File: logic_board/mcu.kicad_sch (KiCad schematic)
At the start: 4 parts, among them J1 SJ3-35083C-TR, J2 SOICBite, U1 STM32H7B0RBTx, U3 MCP73832-2-OT

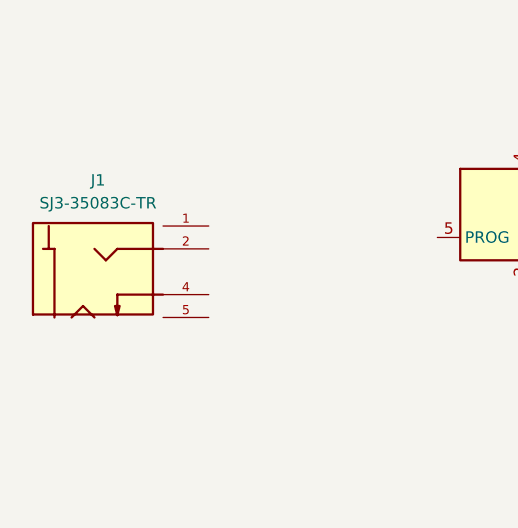
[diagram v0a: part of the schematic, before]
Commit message: Create a pin mapping file
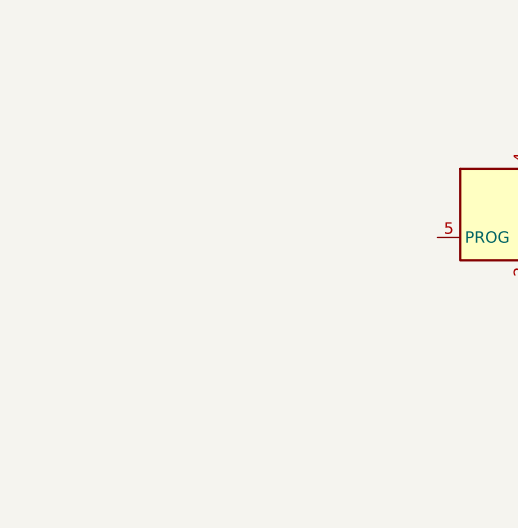
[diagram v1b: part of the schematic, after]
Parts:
- removed J1: SJ3-35083C-TR, Custom_Footprints:SAMESKY_SJ3-35083C-TR, symbol Custom_Symbols:SJ3-35083C-TR
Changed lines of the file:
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@@
-	)
-	(symbol
-		(lib_id "Custom_Symbols:SJ3-35083C-TR")
-		(at 40.64 63.5 0)
-		(unit 1)
-		(exclude_from_sim no)
-		(in_bom yes)
-		(on_board yes)
-		(dnp no)
-		(fields_autoplaced yes)
-		(property "Reference" "J1"
-			(at 38.4934 53.34 0)
-			(effects
-				(font
-					(size 1.27 1.27)
-				)
-			)
-		)
-		(property "Value" "SJ3-35083C-TR"
-			(at 38.4934 55.88 0)
-			(effects
-				(font
-					(size 1.27 1.27)
-				)
-			)
-		)
-		(property "Footprint" "Custom_Footprints:SAMESKY_SJ3-35083C-TR"
-			(at 40.64 63.5 0)
-			(effects
-				(font
-					(size 1.27 1.27)
-				)
-				(justify bottom)
-				(hide yes)
-			)
-		)
-		(property "Datasheet" "https://www.sameskydevices.com/product/resource/sj3-3508x.pdf"
-			(at 40.64 63.5 0)
-			(effects
-				(font
-					(size 1.27 1.27)
-				)
-				(hide yes)
-			)
-		)
-		(property "Description" "3.5mm Audio Jack"
-			(at 40.64 63.5 0)
-			(effects
-				(font
-					(size 1.27 1.27)
-				)
-				(hide yes)
-			)
-		)
-		(property "PARTREV" "1.01"
-			(at 40.64 63.5 0)
-			(effects
-				(font
-					(size 1.27 1.27)
-				)
-				(justify bottom)
-				(hide yes)
-			)
-		)
-		(property "STANDARD" "Manufacturer Recommendations"
-			(at 40.64 63.5 0)
-			(effects
-				(font
-					(size 1.27 1.27)
-				)
-				(justify bottom)
-				(hide yes)
-			)
-		)
-		(property "MAXIMUM_PACKAGE_HEIGHT" "5.3mm"
-			(at 40.64 63.5 0)
-			(effects
-				(font
-					(size 1.27 1.27)
-				)
-				(justify bottom)
-				(hide yes)
-			)
-		)
-		(property "MANUFACTURER" "Same Sky"
-			(at 40.64 63.5 0)
-			(effects
-				(font
-					(size 1.27 1.27)
-				)
-				(justify bottom)
-				(hide yes)
-			)
-		)
-		(pin "1"
-		)
-		(pin "2"
-		)
-		(pin "4"
-		)
-		(pin "5"
-		)
-		(instances
-			(project "logic_board"
-				(path "/b7b37fe1-b409-497a-9440-d94d882f6459/bab78c00-64d8-4e72-b9b2-c8e2bf935ca1"
-					(reference "J1")
-					(unit 1)
-				)
-			)
-		)
 	)
 	(symbol

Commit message: Add more parts to schematic
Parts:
- added J3: USB_C_Receptacle_USB2.0_16P, Custom_Footprints:TYPE-C-31-M-12, symbol Connector:USB_C_Receptacle_USB2.0_16P
- added J5: Conn_01x02, Connector_JST:JST_PH_B2B-PH-SM4-TB_1x02-1MP_P2.00mm_Vertical, symbol Connector_Generic:Conn_01x02
- added SW1, SW2, SW3, SW4: SW_Push, Button_Switch_SMD:SW_SPST_PTS645Sx43SMTR92, symbol Switch:SW_Push
- added SW5: SW_SPDT, Custom_Footprints:Alps Alpine SSSS211603, symbol Switch:SW_SPDT
- added U4: AP2112K-3.3, Package_TO_SOT_SMD:SOT-23-5, symbol Regulator_Linear:AP2112K-3.3
- added Y1: Crystal_GND24, Crystal:Crystal_SMD_3225-4Pin_3.2x2.5mm, symbol Device:Crystal_GND24
- J2: now left out of the parts list
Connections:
- new net: J3.A1 (GND), J3.A12 (GND), J3.B1 (GND), J3.B12 (GND)
- new net: J3.A4 (VBUS), J3.A9 (VBUS), J3.B4 (VBUS), J3.B9 (VBUS)
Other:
- moved on the sheet: U3

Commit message: Board and symbol updates.
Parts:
- SW5: LCSC part number (none) -> SSSS211603
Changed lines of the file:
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@@
+			)
+		)
+		(property "LCSC part number" "SSSS211603"
+			(at 110.49 121.92 0)
+			(effects
+				(font
+					(size 1.27 1.27)
+				)
+				(hide yes)
 			)
 		)

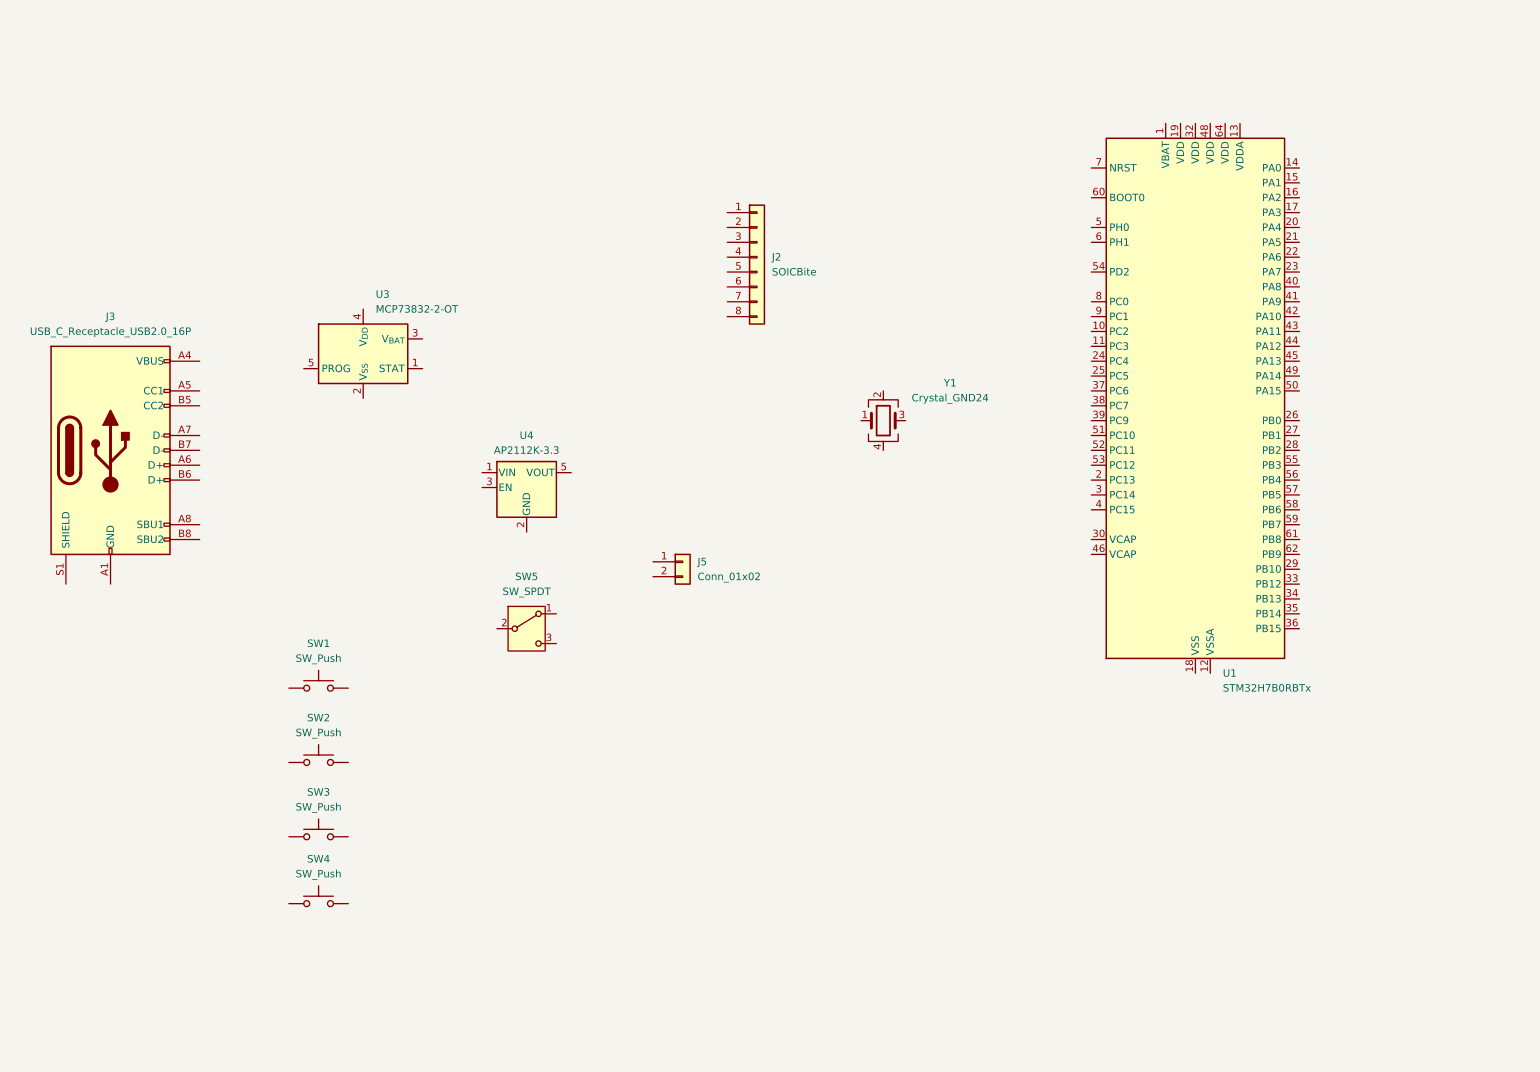
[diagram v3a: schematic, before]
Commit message: Ready for routing. - Lay out all components in proper positions - Add all support passives (bypass caps, etc) - Add board corner cutouts for enclosure bosses.
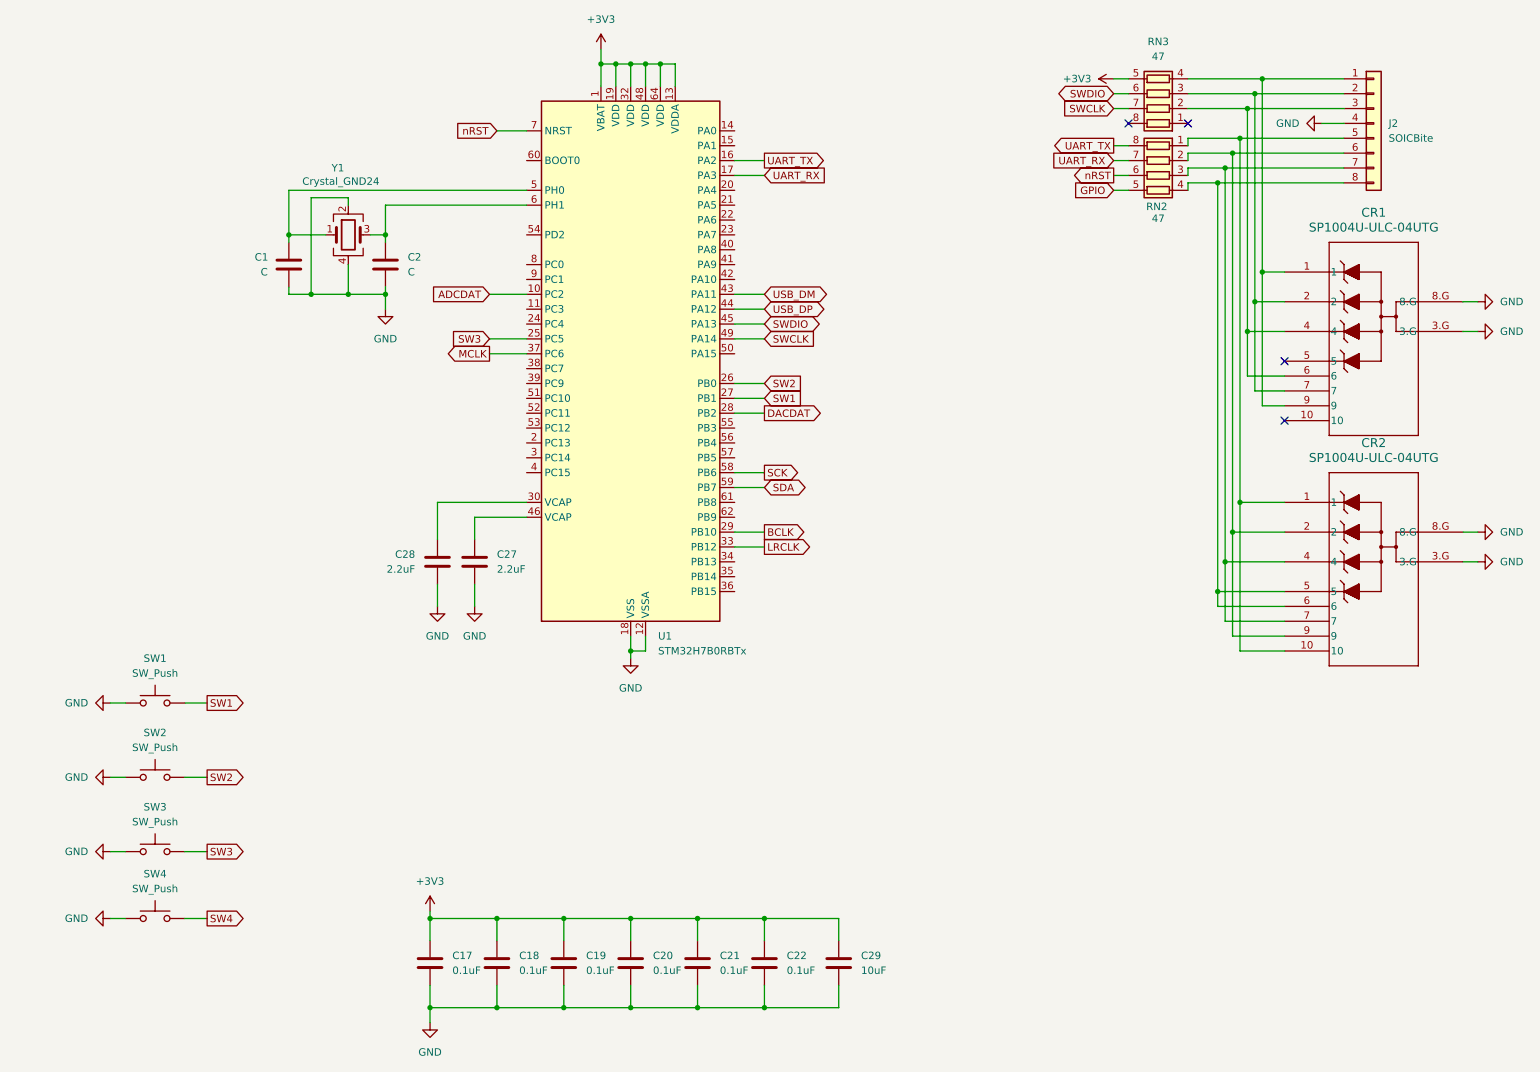
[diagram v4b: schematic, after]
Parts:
- removed J3: USB_C_Receptacle_USB2.0_16P, Custom_Footprints:TYPE-C-31-M-12, symbol Connector:USB_C_Receptacle_USB2.0_16P
- removed J5: Conn_01x02, Connector_JST:JST_PH_B2B-PH-SM4-TB_1x02-1MP_P2.00mm_Vertical, symbol Connector_Generic:Conn_01x02
- removed SW5: SW_SPDT, Custom_Footprints:Alps Alpine SSSS211603, symbol Switch:SW_SPDT
- removed U3: MCP73832-2-OT, Package_TO_SOT_SMD:SOT-23-5, symbol Battery_Management:MCP73832-2-OT
- removed U4: AP2112K-3.3, Package_TO_SOT_SMD:SOT-23-5, symbol Regulator_Linear:AP2112K-3.3
- added C1, C2: C, Capacitor_SMD:C_0603_1608Metric, symbol Device:C
- added C17, C18, C19, C20, C21, C22: 0.1uF, Capacitor_SMD:C_0603_1608Metric, symbol Device:C
- added C27, C28: 2.2uF, Capacitor_SMD:C_0603_1608Metric, symbol Device:C
- added C29: 10uF, Capacitor_SMD:C_0603_1608Metric, symbol Device:C
- added CR1, CR2: SP1004U-ULC-04UTG, Custom_Footprints:1004DFN_LTF, symbol Custom_Symbols:SP1004U-ULC-04UTG
- added RN2, RN3: 47, Resistor_SMD:R_Array_Concave_4x0402, symbol Device:R_Pack04
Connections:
- net at Y1.1: now also U1.5 (PH0), C1.1
- net GND: now reaches Y1.2
- net GND: now also J2.4 (Pin_4), SW1.1, SW2.1, SW3.1, SW4.1, U1.12 (VSSA), U1.18 (VSS), U1.31 (VSS), U1.47 (VSS), U1.63 (VSS), Y1.4, C1.2, C17.2, C18.2, C19.2, C2.2, C20.2, C21.2, C22.2, C27.2, C28.2, C29.2, CR1.3.G, CR1.8.G, CR2.3.G, CR2.8.G
- net at Y1.3: now also U1.6 (PH1), C2.1
- net +3V3: now reaches U1.1 (VBAT)
- net +3V3: now also U1.13 (VDDA), U1.19 (VDD), U1.32 (VDD), U1.48 (VDD), U1.64 (VDD), C17.1, C18.1, C19.1, C20.1, C21.1, C22.1, C29.1, RN3.5 (R4.2)
- net ADCDAT: now reaches U1.10 (PC2)
- net UART_TX: now reaches U1.16 (PA2)
- net UART_TX: now also RN2.8 (R1.2)
- net UART_RX: now reaches U1.17 (PA3)
- net UART_RX: now also RN2.7 (R2.2)
- net SW3: now reaches U1.25 (PC5)
- net SW3: now also SW3.2
- net SW2: now reaches U1.26 (PB0)
- net SW2: now also SW2.2
- net SW1: now reaches U1.27 (PB1)
- net SW1: now also SW1.2
- net DACDAT: now reaches U1.28 (PB2)
- net BCLK: now reaches U1.29 (PB10)
- net at U1.30 (VCAP): now also C28.1
- net LRCLK: now reaches U1.33 (PB12)
- net MCLK: now reaches U1.37 (PC6)
- net USB_DM: now reaches U1.43 (PA11)
- net USB_DP: now reaches U1.44 (PA12)
- net SWDIO: now reaches U1.45 (PA13)
- net SWDIO: now also RN3.6 (R3.2)
- net at U1.46 (VCAP): now also C27.1
- net SWCLK: now reaches U1.49 (PA14)
- net SWCLK: now also RN3.7 (R2.2)
- net SCK: now reaches U1.58 (PB6)
- net SDA: now reaches U1.59 (PB7)
- net nRST: now reaches U1.7 (NRST)
- net nRST: now also RN2.6 (R3.2)
- net SW4: now reaches SW4.2
- net at J2.1 (Pin_1): now also CR1.1, CR1.9, RN3.4 (R4.1)
- net at J2.2 (Pin_2): now also CR1.2, CR1.7, RN3.3 (R3.1)
- net at J2.3 (Pin_3): now also CR1.4, CR1.6, RN3.2 (R2.1)
- net at J2.5 (Pin_5): now also CR2.1, CR2.10, RN2.1 (R1.1)
- net at J2.6 (Pin_6): now also CR2.2, CR2.9, RN2.2 (R2.1)
- net at J2.7 (Pin_7): now also CR2.4, CR2.7, RN2.3 (R3.1)
- net at J2.8 (Pin_8): now also CR2.5, CR2.6, RN2.4 (R4.1)
- new net GPIO: RN2.5 (R4.2)
- no-connect marks 0 -> 4
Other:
- moved on the sheet: J2, SW1, SW2, SW3, SW4, U1, Y1

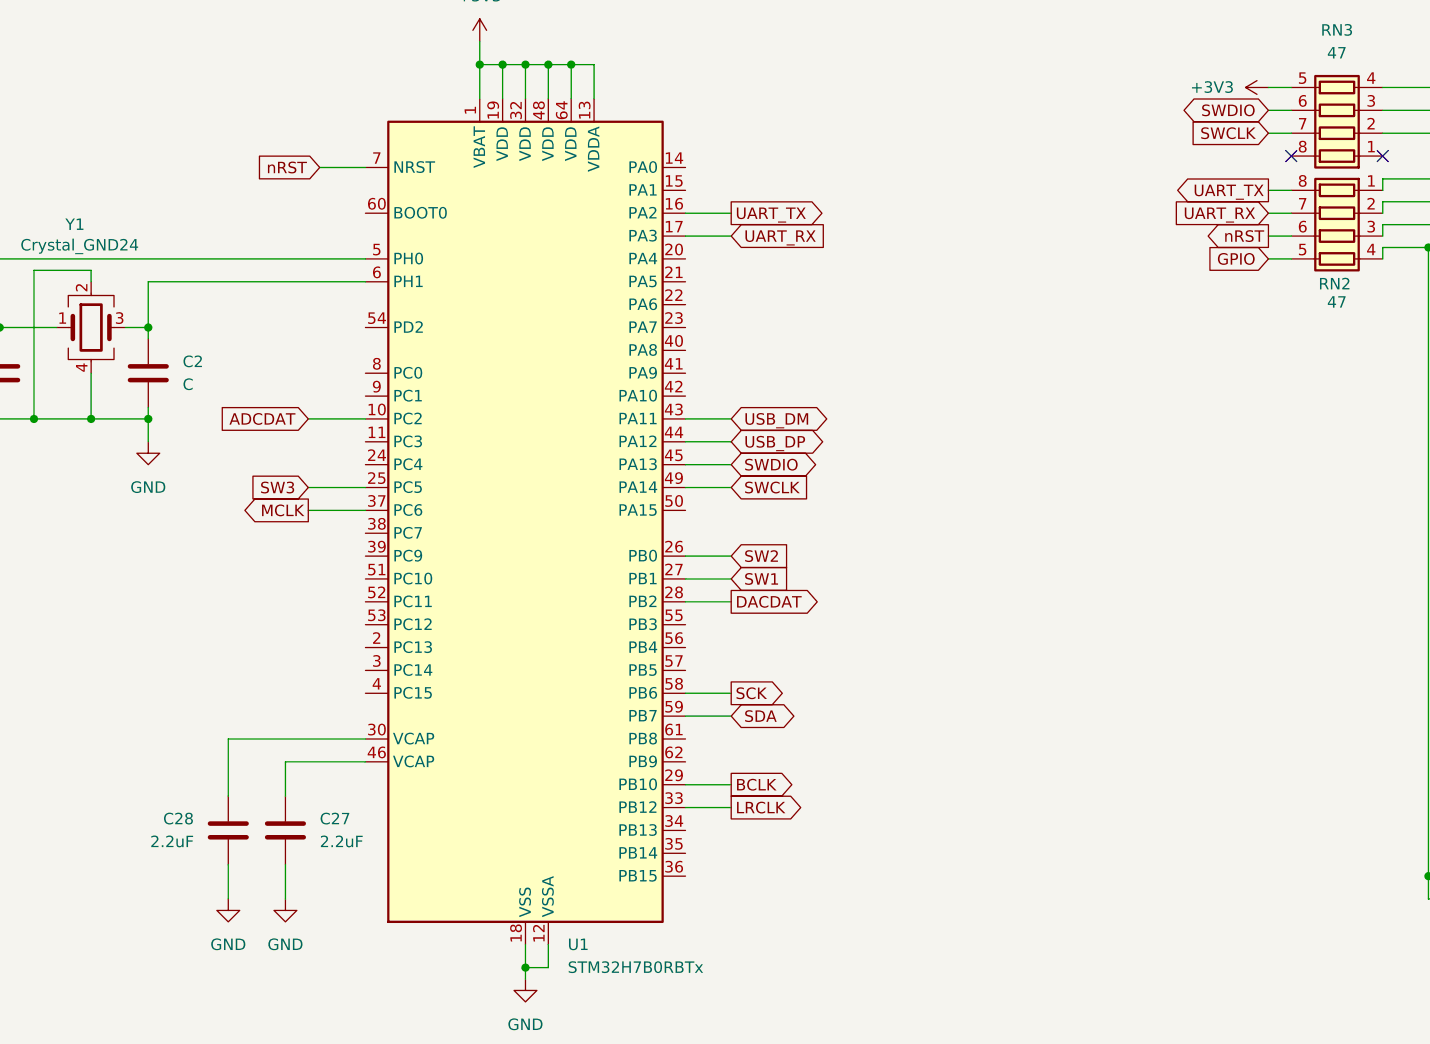
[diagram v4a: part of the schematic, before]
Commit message: Fix DRC and ERC violations
Also updated some design rules to be consistent with fab.
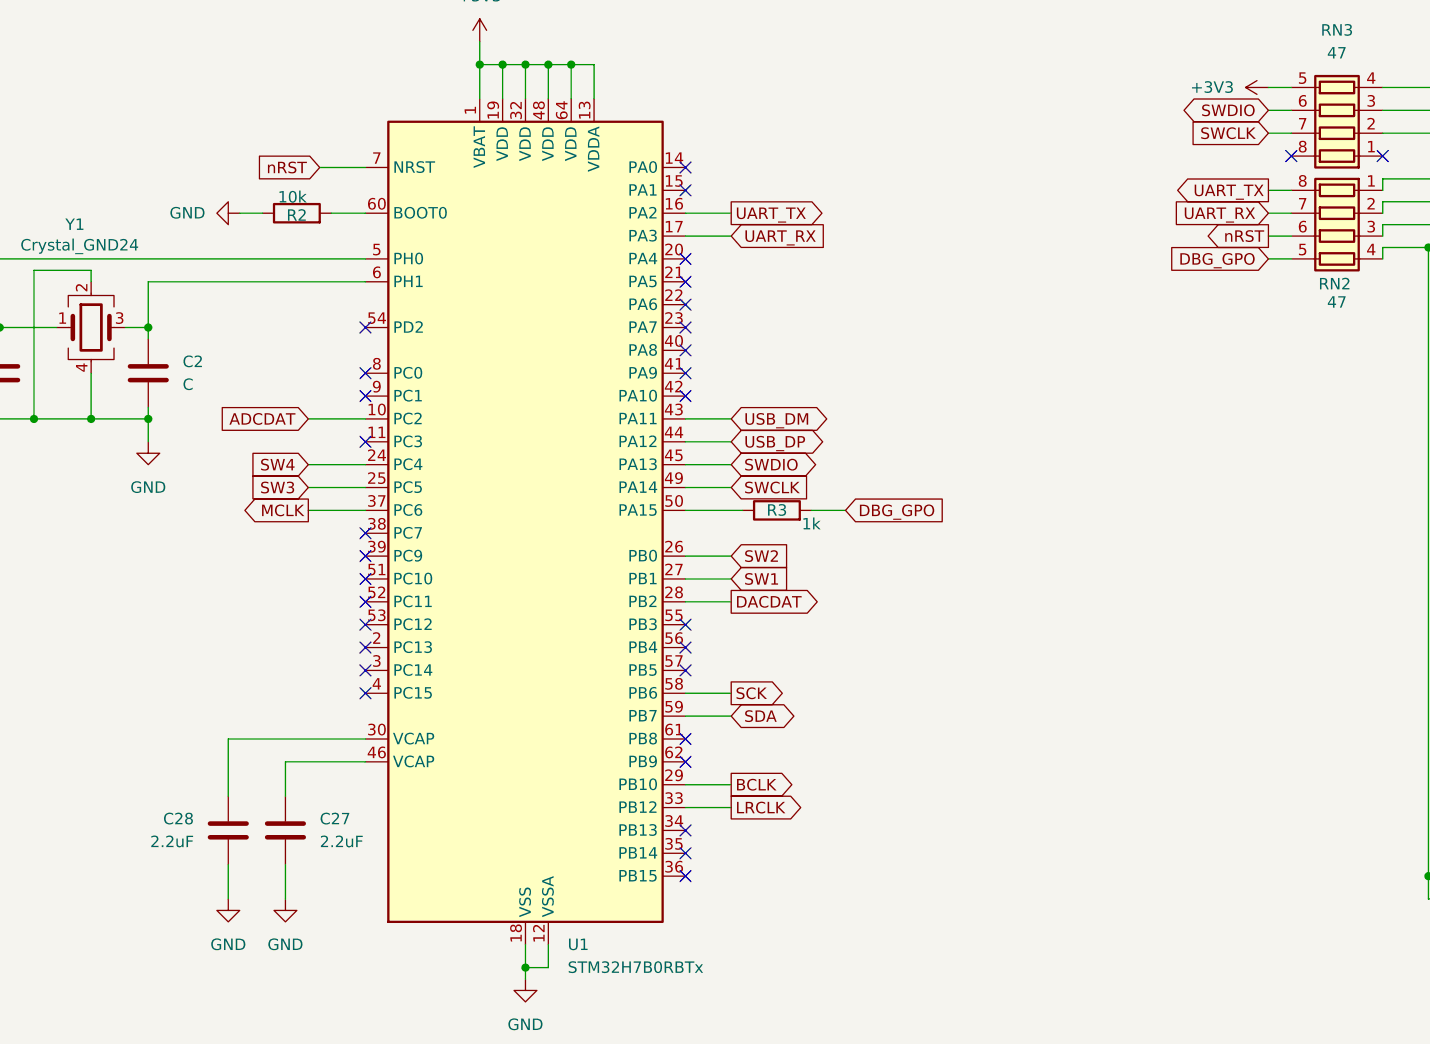
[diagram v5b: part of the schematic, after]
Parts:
- added R2: 10k, Resistor_SMD:R_0603_1608Metric, symbol Device:R
- added R3: 1k, Resistor_SMD:R_0603_1608Metric, symbol Device:R
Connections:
- net GND: now also R2.1
- net SW4: now also U1.24 (PC4)
- net at U1.50 (PA15): now also R3.1
- net at U1.60 (BOOT0): now also R2.2
- net GPIO renamed DBG_GPO
- net DBG_GPO: now also R3.2
- no-connect marks 4 -> 33

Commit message: All signals now routed.
A bit rough, needs some cleanup.
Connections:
- net at CR1.4, J2.3 (Pin_3), RN3.2 (R2.1): now also CR1.7; no longer CR1.6
- net at CR1.2, J2.2 (Pin_2), RN3.3 (R3.1): now also CR1.9; no longer CR1.7
- net at CR1.1, J2.1 (Pin_1), RN3.4 (R4.1): now also CR1.10; no longer CR1.9
- no-connect marks 33 -> 32
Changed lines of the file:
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@@
-	)
-	(no_connect
-		(at 240.03 86.36)
 	)
 	(no_connect
@@
 	(wire
 		(pts
-			(xy 234.95 81.28) (xy 234.95 66.04)
+			(xy 233.68 81.28) (xy 240.03 81.28)
+		)
+		(stroke
+			(width 0)
+			(type default)
+		)
+	)
+	(wire
+		(pts
+			(xy 234.95 66.04) (xy 234.95 83.82)
 		)
 		(stroke
@@
 	(wire
 		(pts
-			(xy 234.95 81.28) (xy 240.03 81.28)
-		)
-		(stroke
-			(width 0)
-			(type default)
-		)
-	)
-	(wire
-		(pts
 			(xy 228.6 45.72) (xy 250.19 45.72)
 		)
@@
 	(wire
 		(pts
-			(xy 236.22 83.82) (xy 240.03 83.82)
-		)
-		(stroke
-			(width 0)
-			(type default)
-		)
-	)
-	(wire
-		(pts
 			(xy 270.51 110.49) (xy 273.05 110.49)
 		)
@@
 	(wire
 		(pts
+			(xy 240.03 86.36) (xy 236.22 86.36)
+		)
+		(stroke
+			(width 0)
+			(type default)
+		)
+	)
+	(wire
+		(pts
 			(xy 105.41 171.45) (xy 116.84 171.45)
 		)
@@
 	(wire
 		(pts
-			(xy 233.68 78.74) (xy 240.03 78.74)
+			(xy 240.03 83.82) (xy 234.95 83.82)
 		)
 		(stroke
@@
 	(wire
 		(pts
-			(xy 233.68 78.74) (xy 233.68 71.12)
-		)
-		(stroke
-			(width 0)
-			(type default)
-		)
-	)
-	(wire
-		(pts
-			(xy 236.22 83.82) (xy 236.22 60.96)
-		)
-		(stroke
+			(xy 233.68 71.12) (xy 233.68 81.28)
+		)
+		(stroke
+			(width 0)
+			(type default)
+		)
+	)
+	(wire
+		(pts
+			(xy 236.22 60.96) (xy 236.22 86.36)
+		)
+		(stroke
